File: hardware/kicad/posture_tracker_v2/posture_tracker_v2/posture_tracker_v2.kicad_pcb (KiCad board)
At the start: 2 copper layers, 45 x 35 mm, 47 parts, among them J1 HRO TYPE-C-31-M-12, J2 JST-PH-2, J3 Conn_01x02, SW1 BTN_CAL, SW2 BTN_SNOOZE, SW3 RESET, U1 ESP32-S3-MINI-1, U2 MPU-6050, U3 DRV2605LDGS, U4 MAX98357A, U5 MCP73831T-2ACI/OT, U6 AP2112K-3.3TRG1, U7 USBLC6-2SC6

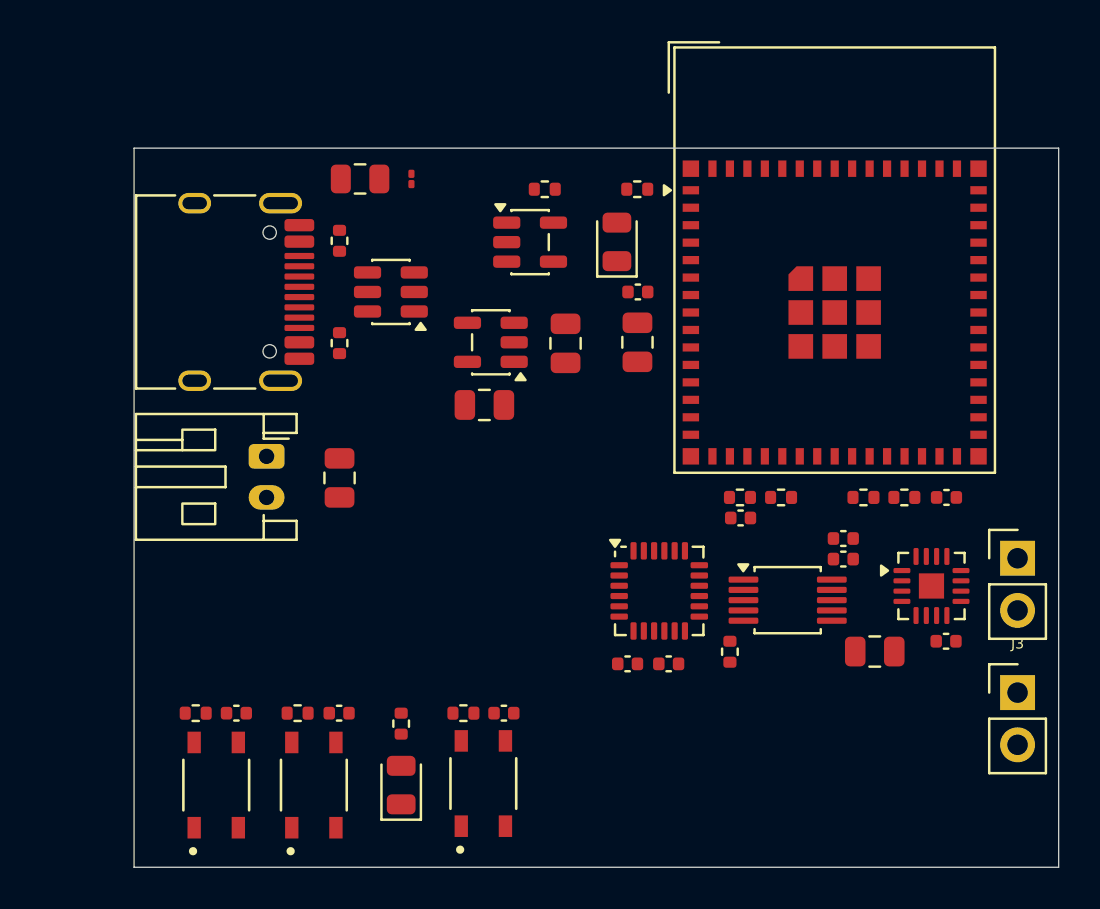
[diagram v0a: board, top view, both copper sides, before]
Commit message: WIP: PCB layout routing setup — clean DRC baseline, connector updates
- PCB: cleared all routing, established clean DRC baseline (154 unconnected,
  2 acceptable silk warnings for U1 antenna overhang, 0 copper errors)
- PCB: GND routing strategy decided — B.Cu copper pour filled at end,
  no manual GND traces; Power/Default net classes configured
- Schematic: J3 (LRA) and LS1 (speaker) connector footprints set to
  JST GH 1.25mm vertical to match physical cable connectors on
  Vybronics LRA and MECCANIXITY 20mm speaker
- .gitignore: added DS_Store, KiCad lock/backup/temp files, KiCad plot PDFs
- README_V2.md: updated Phase 10 status, added PCB layout state section
- hardware/pcb/README.md: updated routing progress tracker
- hardware/schematics/README.md: added connector decision table

Routing order: +3V3 → VBAT → VBUS → I2C → I2S → USB → signals → GND pour

Co-Authored-By: Claude Sonnet 4.6 <noreply@anthropic.com>
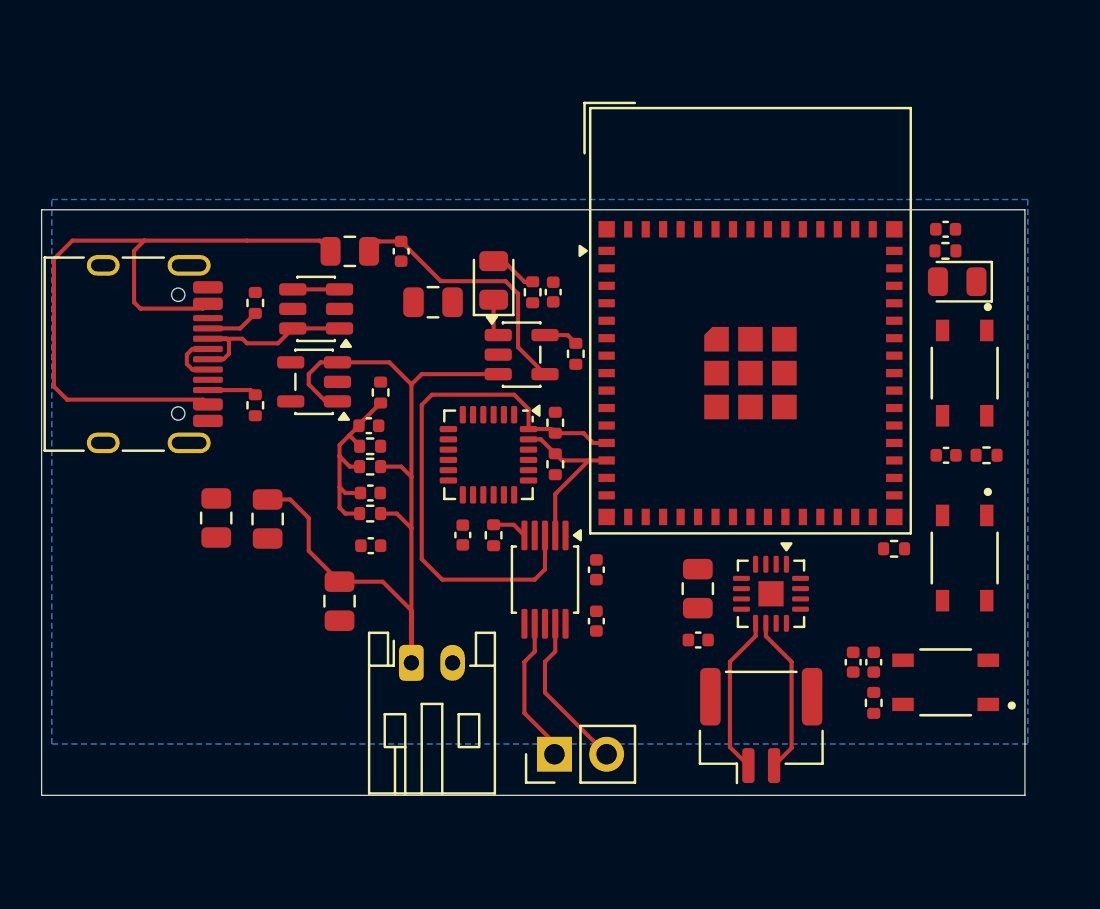
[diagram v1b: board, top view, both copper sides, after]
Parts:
- removed the C10 at (204.5, 117.0)
- removed the R10 at (202.5, 117.0)
- removed the R9 at (200.5, 117.0)
- added C10: 100n, Capacitor_SMD:C_0402_1005Metric, F.Cu at (176.5, 116.8)
- added C10: 100n, Capacitor_SMD:C_0402_1005Metric, F.Cu at (176.4, 113.5)
- added R10: 100k, Resistor_SMD:R_0402_1005Metric, F.Cu at (176.5, 114.5)
- added R10: 100k, Resistor_SMD:R_0402_1005Metric, F.Cu at (177.0, 111.9)
- added R9: 100k, Resistor_SMD:R_0402_1005Metric, F.Cu at (176.5, 115.5)
- added R9: 100k, Resistor_SMD:R_0402_1005Metric, F.Cu at (176.5, 117.8)
- C17: footprint Capacitor_SMD:C_01005_0402Metric -> Capacitor_SMD:C_0402_1005Metric
- LS1: footprint Connector_PinHeader_2.54mm:PinHeader_1x02_P2.54mm_Vertical -> Connector_JST:JST_GH_BM02B-GHS-TBT_1x02-1MP_P1.25mm_Vertical
- moved LED2 36.5 mm to (205.1, 106.5), turned to 180 degrees
- moved SW1 35.9 mm to (204.5, 126.0), turned to 180 degrees
- moved R8 35.8 mm to (206.5, 115.0), turned to 0 degrees
- moved SW2 33.5 mm to (205.4, 120.0), turned to -90 degrees
- moved R7 33.0 mm to (201.0, 127.0), turned to -90 degrees
- moved R11 32.5 mm to (204.5, 105.0), turned to 0 degrees
- moved C9 32.1 mm to (204.5, 115.0), turned to 0 degrees
- moved C11 31.9 mm to (204.5, 104.0)
- moved C8 31.1 mm to (201.0, 125.0), turned to -90 degrees
- moved SW3 30.8 mm to (205.4, 111.0), turned to -90 degrees
- moved R13 25.5 mm to (202.0, 119.5), turned to 180 degrees
- moved J3 22.7 mm to (185.5, 129.5), turned to 90 degrees
- moved C6 16.8 mm to (171.5, 118.0)
- moved LS1 14.9 mm to (195.5, 128.1)
- moved C7 14.2 mm to (169.0, 118.0), turned to -90 degrees
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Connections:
- J1 pad B6: /USB_DM -> /USB_DP
- J1 pad B7: /USB_DP -> /USB_DM
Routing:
- net /VBAT: track 0.00 -> 42.1 mm
- net /VBUS: track 0.00 -> 35.1 mm
- net /SDA: track 0.00 -> 26.5 mm
- net /VBUS_FUSED: track 0.00 -> 13.0 mm
- net /VBAT_SENSE: track 0.00 -> 10.1 mm
- net /USB_DM: track 0.00 -> 9.62 mm
- net /SCL: track 0.00 -> 8.55 mm
- net /SPK_P: track 0.00 -> 7.81 mm
- net /LRA_N: track 0.00 -> 7.80 mm
- net /SPK_N: track 0.00 -> 7.79 mm
- net /LRA_P: track 0.00 -> 7.16 mm
- net /USB_DP: track 0.00 -> 5.01 mm
- net Net-(J1-CC1): track 0.00 -> 2.61 mm
- net Net-(J1-CC2): track 0.00 -> 2.40 mm
- net Net-(LED1-A): track 0.00 -> 2.32 mm
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- added copper zone on B.Cu, net GND
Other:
- board size 45 x 35 mm -> 47.9 x 28.5 mm

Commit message: V2: clear all PCB traces — restart routing from scratch
Removed all 127 routed segments. Footprints, copper zones, board
outline, and net assignments are preserved. Ratsnest is now the
full unrouted state.

Co-Authored-By: Claude Sonnet 4.6 <noreply@anthropic.com>
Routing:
- net /VBAT: track 42.1 -> 0.00 mm
- net /VBUS: track 35.1 -> 0.00 mm
- net /SDA: track 26.5 -> 0.00 mm
- net /VBUS_FUSED: track 13.0 -> 0.00 mm
- net /VBAT_SENSE: track 10.1 -> 0.00 mm
- net /USB_DM: track 9.62 -> 0.00 mm
- net /SCL: track 8.55 -> 0.00 mm
- net /SPK_P: track 7.81 -> 0.00 mm
- net /LRA_N: track 7.80 -> 0.00 mm
- net /SPK_N: track 7.79 -> 0.00 mm
- net /LRA_P: track 7.16 -> 0.00 mm
- net /USB_DP: track 5.01 -> 0.00 mm
- net Net-(J1-CC1): track 2.61 -> 0.00 mm
- net Net-(J1-CC2): track 2.40 -> 0.00 mm
- net Net-(LED1-A): track 2.32 -> 0.00 mm
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
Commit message: V2: update PCB footprints and 3D models for LS1 and M1
LS1 and M1 footprints updated in PCB from old connectors to
Molex PicoBlade 53047-0210 (1x02, 1.25mm vertical).
3D model assigned: Molex_PicoBlade_53398-0271_1x02-1MP_P1.25mm_Vertical.step
Schematic 4-char value fix included.

Co-Authored-By: Claude Sonnet 4.6 <noreply@anthropic.com>
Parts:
- added C18: 220p, Capacitor_SMD:C_0805_2012Metric, F.Cu at (163.6, 124.0)
- added C19: 220p, Capacitor_SMD:C_0805_2012Metric, F.Cu at (190.0, 128.0)
- added FB1: FerriteBead_Small, Inductor_SMD:L_01005_0402Metric, F.Cu at (162.3, 126.0)
- added R14: 1M, Resistor_SMD:R_0402_1005Metric, F.Cu at (201.0, 121.5)
- LS1: value Conn_01x02 -> Molex_PicoBlade_53047-0210; footprint Connector_JST:JST_GH_BM02B-GHS-TBT_1x02-1MP_P1.25mm_Vertical -> Connector_Molex:Molex_PicoBlade_53047-0210_1x02_P1.25mm_Vertical
- M1: renamed from J3; value Conn_01x02 -> Molex_PicoBlade_53047-0210; footprint Connector_PinHeader_2.54mm:PinHeader_1x02_P2.54mm_Vertical -> Connector_Molex:Molex_PicoBlade_53047-0210_1x02_P1.25mm_Vertical
- moved J2 13.2 mm to (167.0, 118.5), turned to -90 degrees
- moved M1 11.2 mm to (175.8, 124.0), turned to 0 degrees
- moved C14 4.97 mm to (170.5, 120.0)
- moved C6 3.26 mm to (174.0, 116.0)
- moved C7 3.26 mm to (171.5, 115.9)
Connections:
- U4 pad 10: /SPK_N -> Net-(U4-OUTN)
- U4 pad 9: /SPK_P -> Net-(U4-OUTP)
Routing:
- net /VBAT: track 0.00 -> 3.71 mm
- net GND: track 0.00 -> 3.67 mm

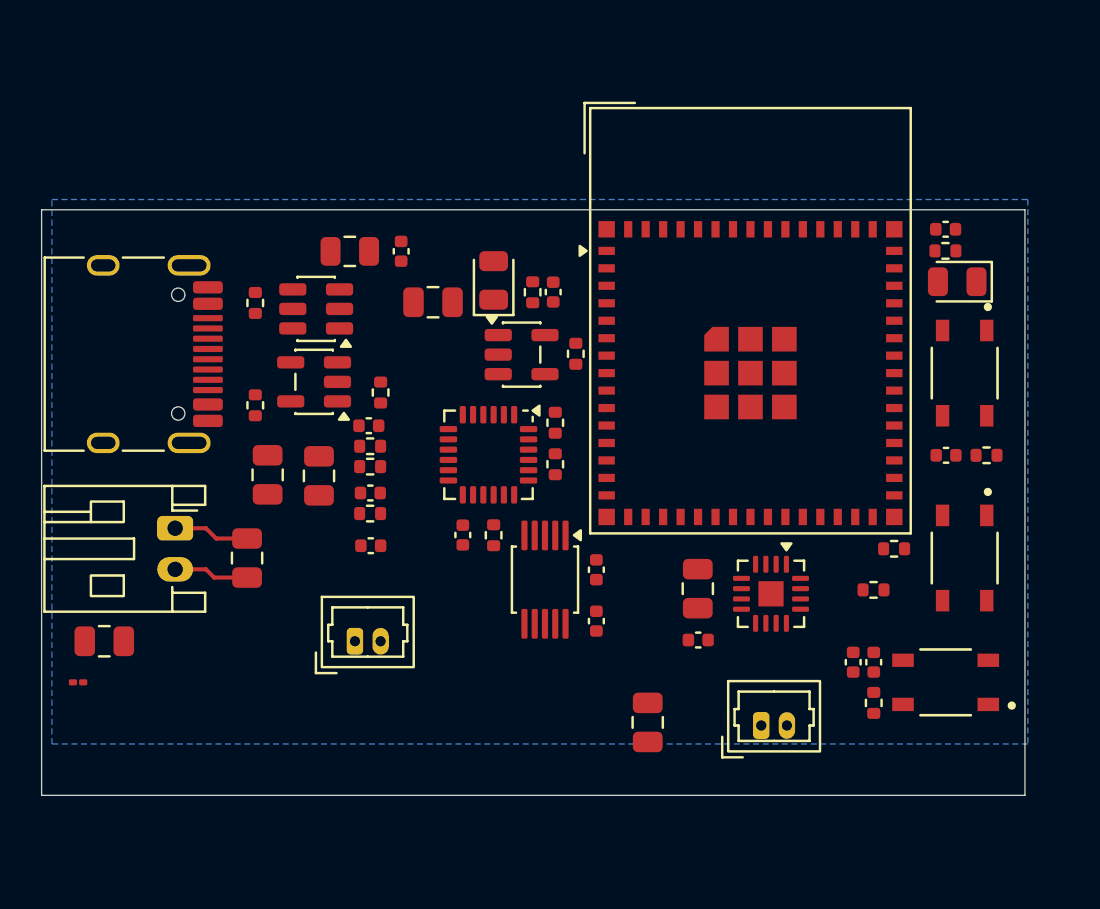
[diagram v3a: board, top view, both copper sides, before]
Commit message: V2: clear all PCB traces — restart routing from scratch
Removed all 7 remaining routed segments. 57 footprints and 13 copper
zones intact. FB1 (ferrite bead) confirmed clean — L_0402_1005Metric
footprint with 0.38mm pad clearance, DRC violation was from a prior
stale placement now resolved.

Board is now a clean ratsnest ready for routing.

Co-Authored-By: Claude Sonnet 4.6 <noreply@anthropic.com>
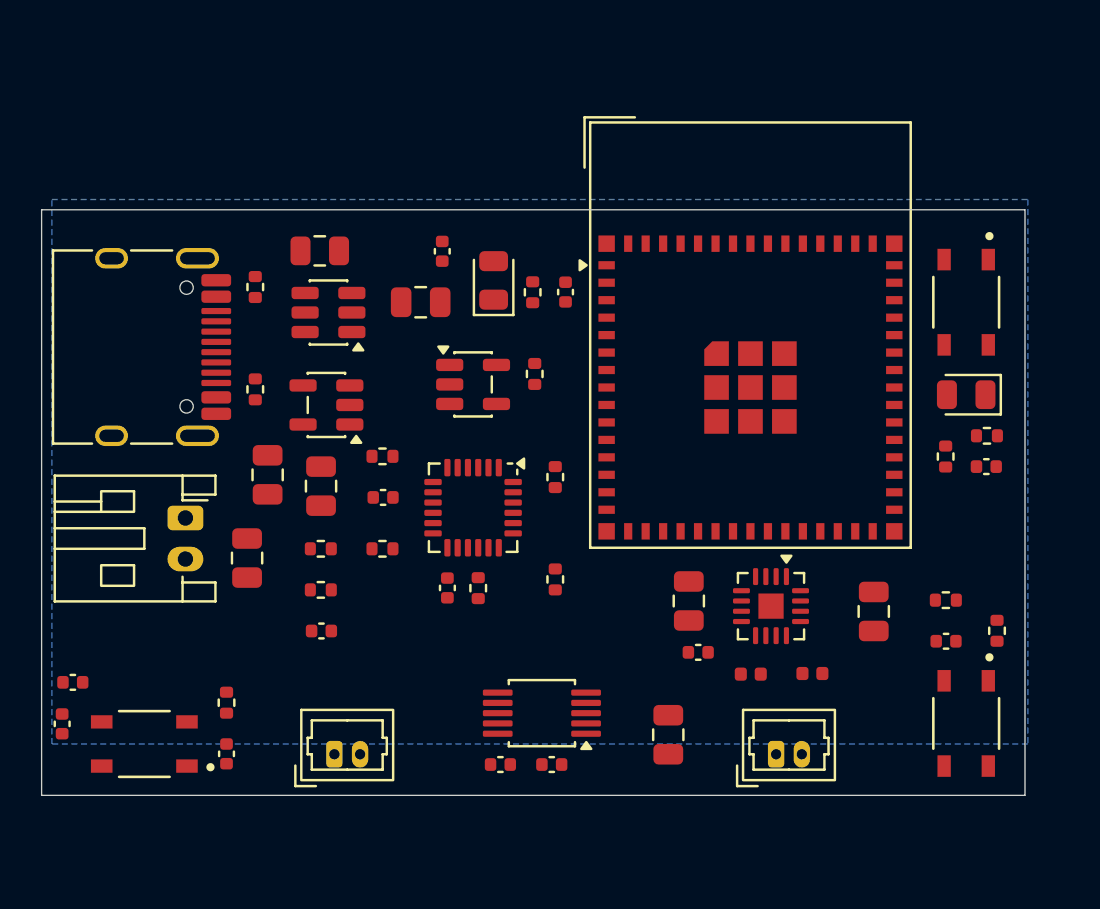
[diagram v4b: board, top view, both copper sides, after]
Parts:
- added FB2: FerriteBead_Small, Inductor_SMD:L_0402_1005Metric, F.Cu at (198.0, 125.6)
- FB1: footprint Inductor_SMD:L_01005_0402Metric -> Inductor_SMD:L_0402_1005Metric
- moved SW1 39.1 mm to (165.5, 129.0)
- moved C16 38.6 mm to (161.5, 128.0)
- moved C18 37.5 mm to (201.0, 122.5), turned to -90 degrees
- moved FB1 32.7 mm to (195.0, 125.6)
- moved C8 31.8 mm to (169.5, 129.5)
- moved R7 31.5 mm to (169.5, 127.0), turned to 90 degrees
- moved C13 16.0 mm to (162.0, 126.0)
- moved C11 11.7 mm to (206.5, 115.5)
- moved C12 9.73 mm to (185.3, 130.0), turned to 180 degrees
- moved R11 9.22 mm to (206.5, 114.0)
- moved C9 9.05 mm to (204.5, 124.0)
- moved C3 8.40 mm to (182.8, 130.0), turned to 0 degrees
- moved SW2 8.05 mm to (205.5, 128.0)
- moved R8 7.32 mm to (204.5, 122.0), turned to 180 degrees
- moved C10 7.12 mm to (174.1, 123.5)
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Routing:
- net /VBAT: track 3.71 -> 0.00 mm
- net GND: track 3.67 -> 0.00 mm

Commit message: V2: PCB routing complete — DRC clean, Gerbers ready for JLCPCB
- All nets fully routed on F.Cu; HAPTIC_EN and MPU_INT via B.Cu
- Trace widths corrected per IPC-2221: VBUS/VBUS_FUSED 0.4mm,
  +3V3/VBAT/audio/motor 0.3mm, signals 0.2mm
- Net classes written to .kicad_pro (HighCurrent, Power, Audio, Motor,
  USB_Diff, Default) with 0.8mm/0.4mm vias across all 19 vias
- F.Cu + B.Cu GND copper fills with solid pad connection + stitching vias
- Final DRC: 0 errors, 0 unconnected, 2 cosmetic silk warnings only
- Gerbers exported to hardware/pcb/v2/gerbers/ (10 layers + 2 drill files)
- ZIP ready: hardware/pcb/v2/posture_tracker_v2_gerbers.zip
- Hardware folder structure reorganised: KiCad source in hardware/kicad/,
  fab outputs in hardware/pcb/v2/, reports in posture_tracker_v2/reports/
- CLAUDE.md Section 18 added: PCB trace width reference, net classes,
  component placement rules, layer strategy
- All docs updated: README_V2, PHASES_V2, KICAD_CONTEXT, hardware READMEs,
  CLAUDE_V2 — Phase 10 design marked complete, awaiting JLCPCB order
- PCB 3D render, top view, and schematic screenshots added to hardware/assets/

Co-Authored-By: Claude Sonnet 4.6 <noreply@anthropic.com>
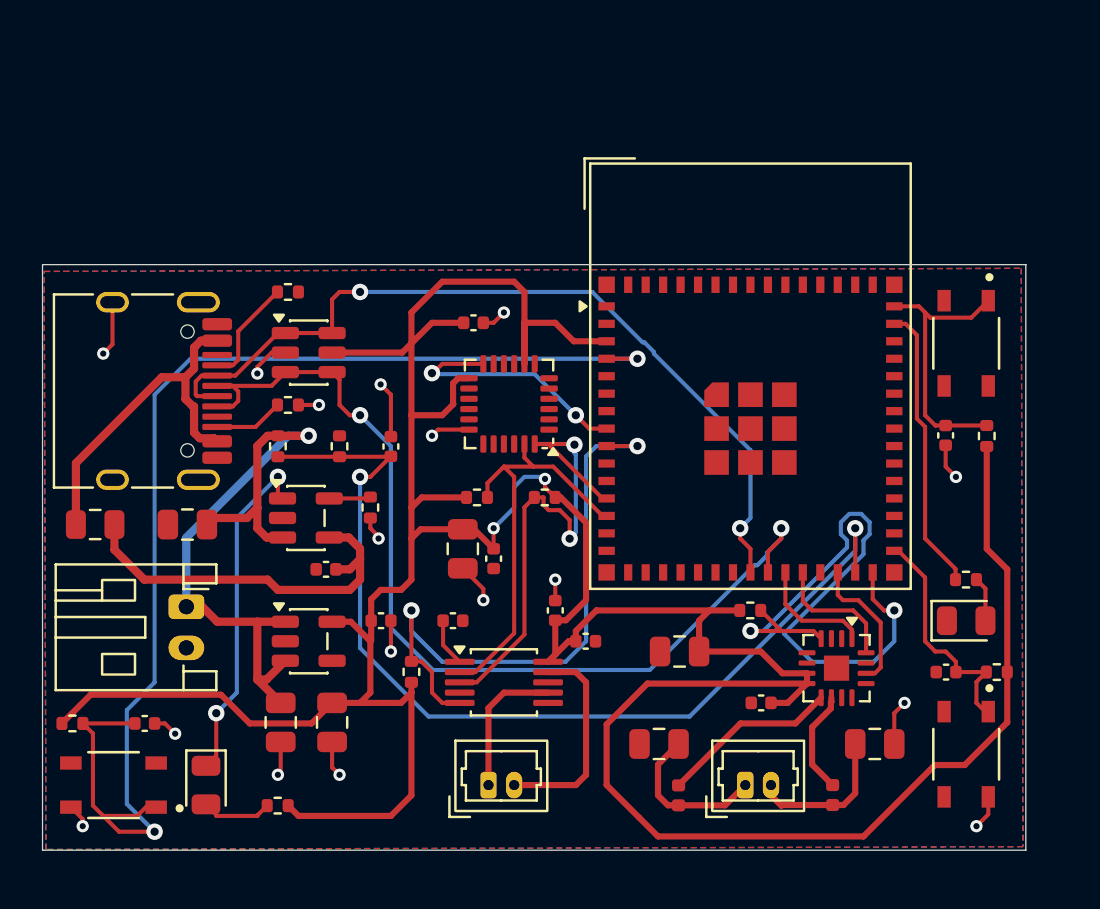
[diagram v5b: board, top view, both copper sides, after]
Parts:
- removed the C10 at (174.1, 123.5)
- removed the C10 at (177.1, 117.0)
- removed the R10 at (177.1, 119.5)
- removed the R10 at (177.1, 115.0)
- removed the R9 at (174.1, 119.5)
- added C10: 100n, Capacitor_SMD:C_0402_1005Metric, F.Cu at (177.5, 114.5)
- added R10: 100k, Resistor_SMD:R_0402_1005Metric, F.Cu at (175.0, 114.5)
- moved LED1 28.3 mm to (168.5, 131.0), turned to -90 degrees
- moved R6 27.9 mm to (172.0, 132.0), turned to 0 degrees
- moved C16 24.6 mm to (185.5, 122.5), turned to -90 degrees
- moved F1 17.2 mm to (163.1, 118.3)
- moved C17 16.5 mm to (174.3, 120.5), turned to 0 degrees
- moved C13 15.3 mm to (177.0, 123.0)
- moved C1 13.4 mm to (182.5, 120.0), turned to -90 degrees
- moved C2 13.0 mm to (181.5, 108.5), turned to 0 degrees
- moved C7 12.5 mm to (174.6, 128.0)
- moved C18 12.3 mm to (190.6, 129.0), turned to 0 degrees
- moved C15 12.2 mm to (181.0, 119.5), turned to 90 degrees
- moved R14 12.1 mm to (195.0, 122.5), turned to 0 degrees
- moved C6 11.7 mm to (172.1, 128.0)
- moved U6 11.5 mm to (173.5, 124.0), turned to 0 degrees
- moved LED2 11.0 mm to (205.5, 123.0), turned to 0 degrees
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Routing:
- net +3V3: track 0.00 -> 176.3 mm, vias 0 -> 2
- net /BTN_CAL: track 0.00 -> 61.1 mm, vias 0 -> 2
- net /USB_DP: track 0.00 -> 48.0 mm, vias 0 -> 2
- net /VBAT_SENSE: track 0.00 -> 48.0 mm, vias 0 -> 2
- net /USB_DM: track 0.00 -> 41.1 mm, vias 0 -> 2
- net /VBAT: track 0.00 -> 33.6 mm, vias 0 -> 1
- net /AUDIO_SD: track 0.00 -> 32.1 mm, vias 0 -> 2
- net /HAPTIC_EN: track 0.00 -> 30.0 mm, vias 0 -> 2
- net GND: track 0.00 -> 28.7 mm, vias 0 -> 17
- net /SDA: track 0.00 -> 25.6 mm, vias 0 -> 2
- net /SCL: track 0.00 -> 20.9 mm
- net /VBUS_FUSED: track 0.00 -> 18.8 mm
- net /VBUS: track 0.00 -> 17.1 mm
- net /STAT: track 0.00 -> 16.7 mm, vias 0 -> 2
- net /SNOOZE_LED: track 0.00 -> 14.0 mm
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- added copper zone on F.Cu, net GND
